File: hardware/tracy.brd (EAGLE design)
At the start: 100 x 80 mm, 67 parts, among them IC1 SIM900, J1 U.FL, J2 U.FL, Q4 si2305cd, T2 BC846, U1 SPX5205 3v3, U3 TC1014 2V8, Y1 32768Hz CFPX-217 12.5pF

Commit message: daily snapshot
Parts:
- moved C13 0.20 mm to (34.8, 26.4)
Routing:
- net N$42: track 0.00 -> 34.5 mm
- net N$43: track 0.00 -> 32.2 mm
- net SIM_VCC: track 3.80 -> 27.0 mm
- net SIMLOCK_IO: track 0.00 -> 19.5 mm
- net SIMLOCK_RST: track 0.00 -> 16.5 mm
- net SIMLOCK_CLK: track 0.00 -> 15.1 mm
- net N$17: track 0.00 -> 2.84 mm
- net N$19: track 0.00 -> 2.79 mm
- net N$18: track 0.00 -> 2.79 mm
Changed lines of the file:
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@@
 <element name="R15" library="rcl" package="R0805W" value="1k1" x="14.9" y="1.8" rot="R180"/>
 <element name="C12" library="rcl" package="C0805" value="4u7" x="34.8" y="23" rot="R180"/>
-<element name="C13" library="rcl" package="C0805" value="100n" x="34.8" y="26.6" rot="R180"/>
+<element name="C13" library="rcl" package="C0805" value="100n" x="34.8" y="26.4" rot="R180"/>
 <element name="C14" library="rcl" package="C0805" value="22p" x="38.9" y="35.1"/>
 <element name="R17" library="rcl" package="R0805W" value="10k" x="34.8" y="35.1" rot="R180"/>
@@
 <contactref element="U$6" pad="6"/>
 <contactref element="U$6" pad="TH"/>
-<polygon width="0.254" layer="1" isolate="0.254">
+<polygon width="0.254" layer="1" isolate="0.254" thermals="no">
 <vertex x="0.1" y="37.6"/>
 <vertex x="58.2" y="37.6"/>
@@
 <contactref element="U$8" pad="3"/>
 <wire x1="30.45" y1="27" x2="33.85" y2="27" width="0.254" layer="1"/>
-<wire x1="33.85" y1="27" x2="33.85" y2="26.6" width="0.254" layer="1"/>
+<wire x1="33.85" y1="27" x2="33.85" y2="26.4" width="0.254" layer="1"/>
 <contactref element="IC1" pad="30"/>
-<wire x1="33.1" y1="32.1" x2="49.01" y2="34" width="0" layer="19" extent="1-1"/>
-<wire x1="33.85" y1="27" x2="33.1" y2="32.1" width="0" layer="19" extent="1-1"/>
+<wire x1="33.1" y1="32.1" x2="33.1" y2="31.7" width="0.254" layer="1"/>
+<wire x1="33.1" y1="31.7" x2="33.3" y2="31.5" width="0.254" layer="1"/>
+<wire x1="33.3" y1="31.5" x2="35.4" y2="31.5" width="0.254" layer="1"/>
+<wire x1="34.75" y1="27.5" x2="33.85" y2="26.4" width="0.254" layer="1"/>
+<wire x1="49.01" y1="34" x2="49.01" y2="32.11" width="0.254" layer="1"/>
+<wire x1="49.01" y1="32.11" x2="47.8" y2="30.9" width="0.254" layer="1"/>
+<wire x1="47.8" y1="30.9" x2="38.1" y2="30.9" width="0.254" layer="1"/>
+<wire x1="38.1" y1="30.9" x2="37.5" y2="30.3" width="0.254" layer="1"/>
+<wire x1="37.5" y1="30.3" x2="37.5" y2="29" width="0.254" layer="1"/>
+<wire x1="37.5" y1="29" x2="36.6" y2="28.1" width="0.254" layer="1"/>
+<wire x1="36.6" y1="28.1" x2="36.1" y2="28.1" width="0.254" layer="1"/>
+<wire x1="36.1" y1="28.1" x2="35.5" y2="27.5" width="0.254" layer="1"/>
+<wire x1="35.5" y1="27.5" x2="34.75" y2="27.5" width="0.254" layer="1"/>
+<wire x1="37.5" y1="30.3" x2="35.4" y2="31.5" width="0" layer="19" extent="1-1"/>
 </signal>
 <signal name="SIMLOCK_CLK">
@@
 <contactref element="U$18" pad="2"/>
 <contactref element="U$8" pad="4"/>
-<wire x1="35" y1="32.1" x2="43.93" y2="34" width="0" layer="19" extent="1-1"/>
-<wire x1="34.8" y1="29.1" x2="35" y2="32.1" width="0" layer="19" extent="1-1"/>
+<wire x1="43.93" y1="34" x2="43.93" y2="32.53" width="0.254" layer="1"/>
+<wire x1="43.93" y1="32.53" x2="43.3" y2="31.9" width="0.254" layer="1"/>
+<wire x1="43.3" y1="31.9" x2="36.5" y2="31.9" width="0.254" layer="1"/>
+<wire x1="36.5" y1="31.9" x2="36.3" y2="32.1" width="0.254" layer="1"/>
+<wire x1="36.3" y1="32.1" x2="35" y2="32.1" width="0.254" layer="1"/>
+<wire x1="34.8" y1="29.1" x2="36.2" y2="29.1" width="0.254" layer="1"/>
+<wire x1="36.2" y1="29.1" x2="36.5" y2="29.4" width="0.254" layer="1"/>
+<wire x1="36.5" y1="29.4" x2="36.5" y2="31.9" width="0.254" layer="1"/>
 </signal>
 <signal name="SIMLOCK_RST">
@@
 <contactref element="U$18" pad="3"/>
 <contactref element="U$8" pad="6"/>
-<wire x1="35" y1="33.4" x2="46.47" y2="34" width="0" layer="19" extent="1-1"/>
+<wire x1="35" y1="33.4" x2="42.5" y2="33.4" width="0.254" layer="1"/>
+<wire x1="42.5" y1="33.4" x2="43" y2="33.9" width="0.254" layer="1"/>
+<wire x1="43" y1="33.9" x2="43" y2="35.5" width="0.254" layer="1"/>
+<wire x1="43" y1="35.5" x2="43.5" y2="36" width="0.254" layer="1"/>
+<wire x1="43.5" y1="36" x2="46.2" y2="36" width="0.254" layer="1"/>
+<wire x1="46.2" y1="36" x2="46.5" y2="35.7" width="0.254" layer="1"/>
+<wire x1="46.5" y1="35.7" x2="46.5" y2="34.03" width="0.254" layer="1"/>
+<wire x1="46.5" y1="34.03" x2="46.47" y2="34" width="0.254" layer="1"/>
+<wire x1="34.8" y1="29.9" x2="35.8" y2="29.9" width="0.254" layer="1"/>
+<wire x1="35.8" y1="29.9" x2="35.9" y2="30" width="0.254" layer="1"/>
 <wire x1="34.8" y1="29.9" x2="35" y2="33.4" width="0" layer="19" extent="1-1"/>
 </signal>
@@
 <contactref element="U$18" pad="1"/>
 <contactref element="U$8" pad="5"/>
-<wire x1="39.85" y1="35.1" x2="45.2" y2="34" width="0" layer="19" extent="1-1"/>
-<wire x1="35" y1="32.75" x2="39.85" y2="35.1" width="0" layer="19" extent="1-1"/>
-<wire x1="34.8" y1="28.225" x2="35" y2="32.75" width="0" layer="19" extent="1-1"/>
+<wire x1="45.2" y1="34" x2="45.2" y2="32.3" width="0.254" layer="1"/>
+<wire x1="45.2" y1="32.3" x2="44.3" y2="31.4" width="0.254" layer="1"/>
+<wire x1="44.3" y1="31.4" x2="37.2" y2="31.4" width="0.254" layer="1"/>
+<wire x1="37.2" y1="31.4" x2="37" y2="31.2" width="0.254" layer="1"/>
+<wire x1="37" y1="31.2" x2="37" y2="29.2" width="0.254" layer="1"/>
+<wire x1="37" y1="29.2" x2="36.4" y2="28.6" width="0.254" layer="1"/>
+<wire x1="36.4" y1="28.6" x2="35.9" y2="28.6" width="0.254" layer="1"/>
+<wire x1="35.9" y1="28.6" x2="35.5" y2="28.2" width="0.254" layer="1"/>
+<wire x1="35.5" y1="28.2" x2="34.825" y2="28.2" width="0.254" layer="1"/>
+<wire x1="34.825" y1="28.2" x2="34.8" y2="28.225" width="0.254" layer="1"/>
+<wire x1="35" y1="32.75" x2="39.55" y2="32.75" width="0.254" layer="1"/>
+<wire x1="39.55" y1="32.75" x2="39.85" y2="35.1" width="0" layer="19" extent="1-1"/>
+<wire x1="37" y1="31.2" x2="35" y2="32.75" width="0" layer="19" extent="1-1"/>
 </signal>
 <signal name="N$42">
@@
 <contactref element="U$8" pad="1"/>
 <contactref element="IC1" pad="34"/>
-<wire x1="33.1" y1="33.4" x2="33.7475" y2="35.1" width="0" layer="19" extent="1-1"/>
-<wire x1="30.45" y1="31" x2="33.1" y2="33.4" width="0" layer="19" extent="1-1"/>
-<wire x1="43.38" y1="2.9" x2="30.45" y2="31" width="0" layer="19" extent="1-1"/>
+<wire x1="30.45" y1="31" x2="30.45" y2="32.35" width="0.254" layer="1"/>
+<wire x1="30.45" y1="32.35" x2="31.5" y2="33.4" width="0.254" layer="1"/>
+<wire x1="31.5" y1="33.4" x2="33.1" y2="33.4" width="0.254" layer="1"/>
+<wire x1="33.1" y1="33.4" x2="33.1" y2="34.4525" width="0.254" layer="1"/>
+<wire x1="33.1" y1="34.4525" x2="33.7475" y2="35.1" width="0.254" layer="1"/>
+<wire x1="43.38" y1="2.9" x2="43.38" y2="25.52" width="0.254" layer="1"/>
+<wire x1="43.38" y1="25.52" x2="39.5" y2="29.4" width="0.254" layer="1"/>
+<wire x1="39.5" y1="29.4" x2="33.1" y2="33.4" width="0" layer="19" extent="1-1"/>
 </signal>
 <signal name="N$43">
 <contactref element="R17" pad="1"/>
 <contactref element="IC1" pad="15"/>
-<wire x1="25.2" y1="11.75" x2="35.8525" y2="35.1" width="0" layer="19" extent="1-1"/>
+<wire x1="25.2" y1="11.75" x2="25.2" y2="13" width="0.254" layer="1"/>
+<wire x1="25.2" y1="13" x2="28.2" y2="16" width="0.254" layer="1"/>
+<wire x1="28.2" y1="16" x2="28.2" y2="32" width="0.254" layer="1"/>
+<wire x1="28.2" y1="32" x2="32.8" y2="36.6" width="0.254" layer="1"/>
+<wire x1="32.8" y1="36.6" x2="35.3" y2="36.6" width="0.254" layer="1"/>
+<wire x1="35.3" y1="36.6" x2="35.8" y2="36.1" width="0.254" layer="1"/>
+<wire x1="35.8" y1="36.1" x2="35.8" y2="35.1525" width="0.254" layer="1"/>
+<wire x1="35.8" y1="35.1525" x2="35.8525" y2="35.1" width="0.254" layer="1"/>
 </signal>
 <signal name="PWRKEY">
@@
 <contactref element="U$18" pad="8"/>
 <contactref element="IC1" pad="31"/>
-<wire x1="30.45" y1="28" x2="33.2" y2="28.225" width="0" layer="19" extent="1-1"/>
+<wire x1="30.45" y1="28" x2="32.975" y2="28" width="0.254" layer="1"/>
+<wire x1="32.975" y1="28" x2="33.2" y2="28.225" width="0.254" layer="1"/>
 </signal>
 <signal name="N$18">
 <contactref element="U$18" pad="7"/>
 <contactref element="IC1" pad="32"/>
-<wire x1="30.45" y1="29" x2="33.2" y2="29.1" width="0" layer="19" extent="1-1"/>
+<wire x1="30.45" y1="29" x2="33.1" y2="29" width="0.254" layer="1"/>
+<wire x1="33.1" y1="29" x2="33.2" y2="29.1" width="0.254" layer="1"/>
 </signal>
 <signal name="N$19">
 <contactref element="U$18" pad="6"/>
 <contactref element="IC1" pad="33"/>
-<wire x1="30.45" y1="30" x2="33.2" y2="29.9" width="0" layer="19" extent="1-1"/>
+<wire x1="30.45" y1="30" x2="33.1" y2="30" width="0.254" layer="1"/>
+<wire x1="33.1" y1="30" x2="33.2" y2="29.9" width="0.254" layer="1"/>
 </signal>
 <signal name="PW_RAW">

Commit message: pcb done
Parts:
- removed LED3: orange, led:CHIP-LED0805
- removed R9: 10k, rcl:R0805W
- added LED1: green, led:CHIPLED_0805
- added R6: 100k, rcl:R0805W
- added R7: 470, rcl:R0805W
- R14: value NA/10k -> DNP 10k th
- U$17: value battery -> MOLEX_4HORIZONTAL
- U$19: value power_in -> MOLEX_4HORIZONTAL
- U2: value (none) -> 3339
- moved R1 60.5 mm to (38.2, 19.8), turned to 90 degrees
- moved R35 53.2 mm to (23.7, 22.6), turned to 0 degrees
- moved R34 52.8 mm to (24.7, 19.6)
- moved C10 52.4 mm to (5.60, 17.4), turned to 270 degrees
- moved U$20 51.5 mm to (34.4, 14.0)
- moved C17 49.5 mm to (7.70, 17.4), turned to 270 degrees
- moved C8 46.7 mm to (9.80, 17.4), turned to 270 degrees
- moved C24 45.7 mm to (13.0, 12.3), turned to 270 degrees
- moved C7 43.6 mm to (38.2, 15.6), turned to 270 degrees
- moved C23 42.7 mm to (15.1, 12.3), turned to 270 degrees
- moved Y1 42.0 mm to (14.1, 15.5), turned to 180 degrees
- moved U2 40.8 mm to (40.3, 31.5), turned to 180 degrees
- moved C9 40.2 mm to (12.7, 31.1), turned to 180 degrees
- moved R3 39.7 mm to (18.9, 10.9), turned to 180 degrees
- moved R4 37.9 mm to (18.9, 13.0), turned to 0 degrees
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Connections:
- net N$8 renamed GPS_VCC
- removed net N$21: LED3.C, U$6.9
- removed net N$22: LED3.A, R9.2
- removed net P1.0: U$1.14
- removed net P1.1: U$1.15
- removed net P1.2: U$1.16
- removed net P1.3: U$1.17
- removed net P1.4: U$1.18
- removed net P1.5: U$1.19
- removed net P1.6: U$1.20
- removed net P1.7: U$1.21
- removed net P2.0: U$1.22
- removed net P4.6: U$1.35
- removed net P4.7: U$1.36
- removed net P5.0: U$1.5
- removed net P5.1: U$1.6
- removed net P6.0: U$1.1
- removed net P6.1: C18.1, R22.2, R24.1, U$1.2
- removed net P6.2: C2.1, R3.2, R4.1, U$1.3
- removed net P6.3: U$1.4
- new net BAT_DIV: C2.1, R3.2, R4.1, U$1.4
- new net CH: R7.2, U$1.15
- new net N$10: R7.1, U$6.9
- new net N$8: LED1.C, R6.1
- new net PW_RAW_DIV: C18.1, R22.2, R24.1, U$1.3
- new net STATUS: LED1.A, U$1.16
- net 3V3_EN: now also U$1.1
- net 5V: now also U$17.4; no longer U$19.4
- net BAT: now also U$19.1; no longer U$17.4
- net CE: now also U$1.2
- net CTS: now also U$1.19
- net DTR: now also U$1.17
- net GND: now also R6.2, U$19.2; no longer U$17.2
- net GPRS_EN: now also U$1.21
- net GPRS_POW: now also U$1.22
- net N$12: now also U$17.2; no longer U$19.2
- net P4.0: now also U$20.5; no longer U$20.6
- net P4.1: now also U$20.6; no longer U$20.5
- net PW_EN: now also U$1.36
- net PW_RAW: now also U$17.1; no longer U$19.1
- net RI: now also U$1.18
- net RTS: now also U$1.20
- net TS: now also U$19.4; no longer U$17.1
- net VBACKUP: now also U$1.35
- net VIN: no longer R9.1
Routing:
- net 2V8: track 0.00 -> 70.7 mm, vias 0 -> 7
- net PW_EN: track 0.00 -> 38.9 mm
- net VIN: track 33.4 -> 70.6 mm, vias 0 -> 3
- net 3V3_EN: track 0.00 -> 36.2 mm, vias 0 -> 2
- net GPRS_RX: track 0.00 -> 31.5 mm, vias 0 -> 1
- net VBACKUP: track 0.00 -> 30.9 mm
- net GPRS_TX: track 0.00 -> 29.2 mm, vias 0 -> 1
- net GPRS_POW: track 0.00 -> 28.6 mm, vias 0 -> 1
- net GPS_RX: track 0.00 -> 25.8 mm
- net GPS_TX: track 0.00 -> 24.7 mm
- net CE: track 0.00 -> 24.4 mm, vias 0 -> 3
- net P4.0: track 0.00 -> 24.1 mm, vias 0 -> 2
- net P4.1: track 0.00 -> 22.9 mm, vias 0 -> 2
- net GPS_VCC: track 0.00 -> 20.4 mm
- net TEST: track 0.00 -> 19.0 mm, vias 0 -> 1
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- added copper zone on layer 16, net GND
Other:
- board size 100 x 80 mm -> 58.5 x 38 mm

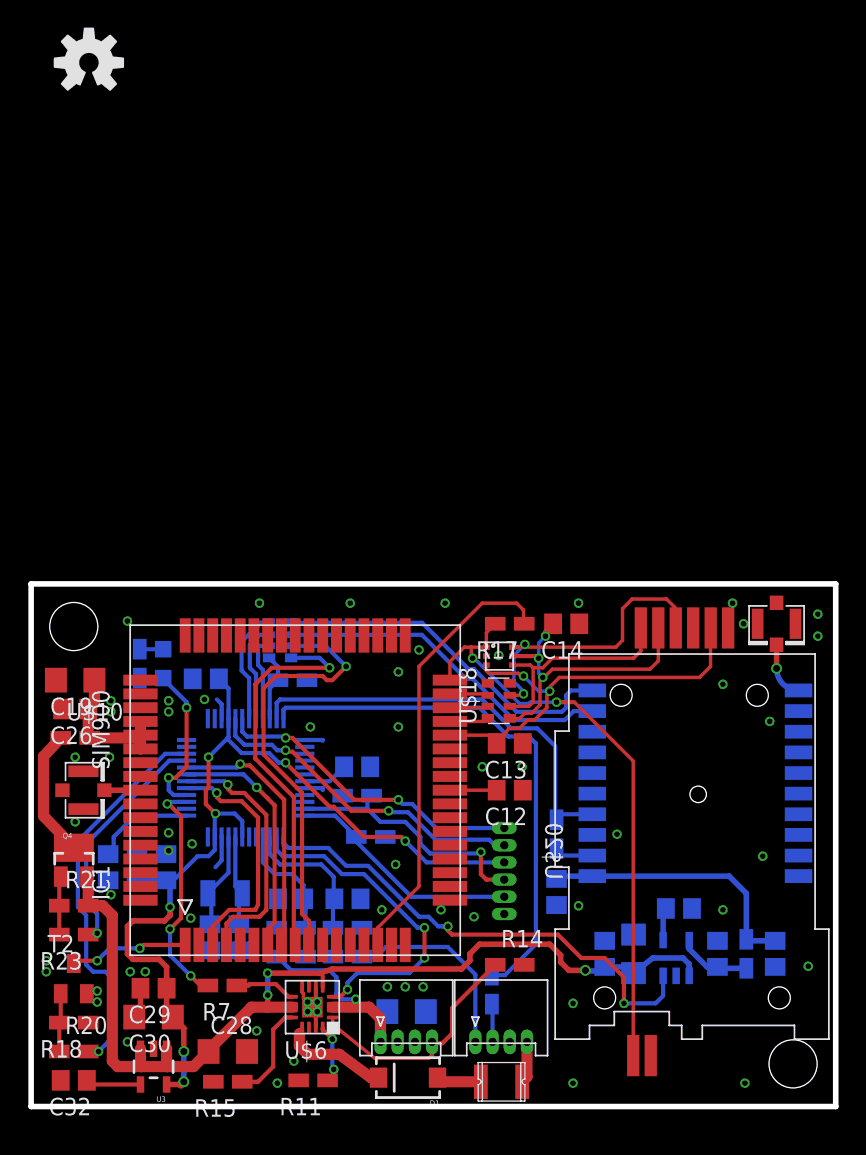
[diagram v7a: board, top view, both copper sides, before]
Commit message: add silkscreen
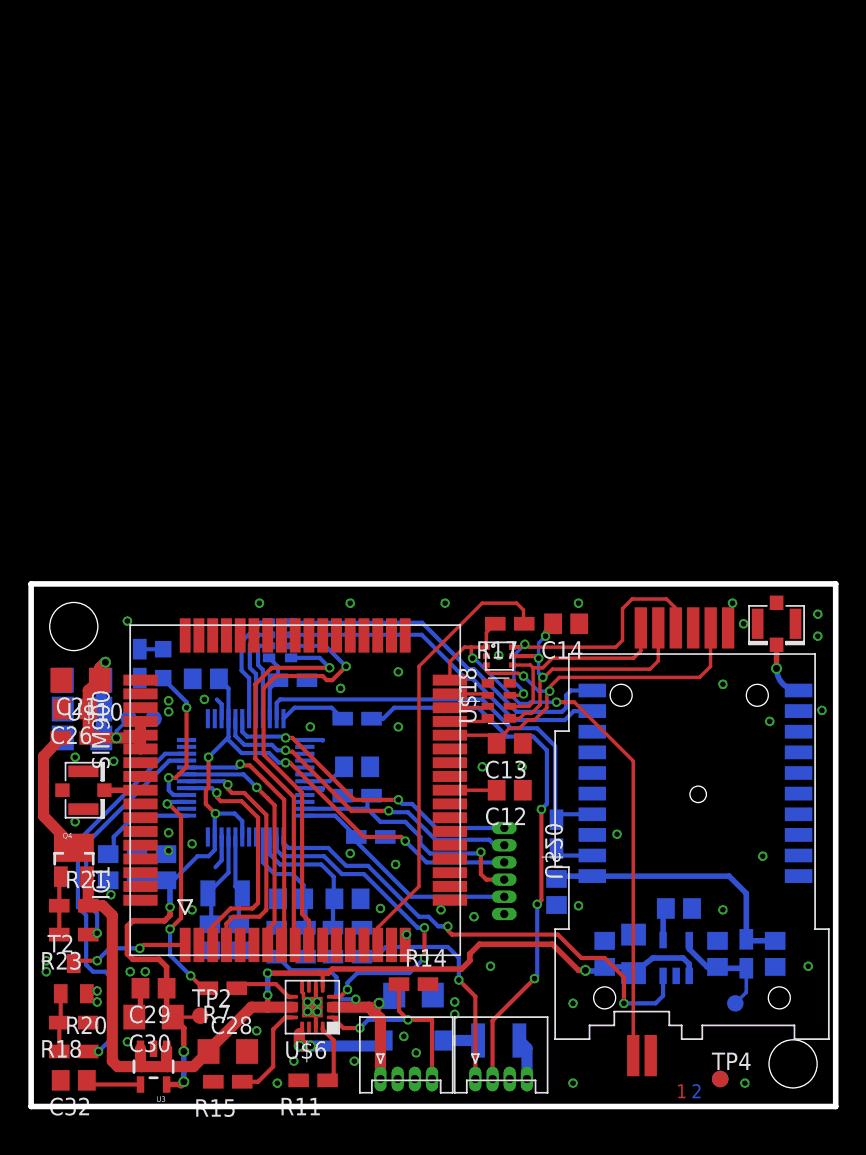
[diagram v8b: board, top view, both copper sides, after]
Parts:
- removed C19: 47uF, rcl:C1206
- added C15, C16, C20, C21: 100uF, rcl:C1206
- added TP1, TP2, TP3, TP4, TP5, TP6: TPTP12R, testpad:TP12R
- U$17: value MOLEX_4HORIZONTAL -> 5V
- U$19: value MOLEX_4HORIZONTAL -> LiPo
- U$20: value MOLEX_6VERTICAL -> prog
- moved U$7 73.7 mm to (34.8, 8.90), flipped to the bottom
- moved R5 22.0 mm to (23.7, 28.2), turned to 0 degrees
- moved R14 7.14 mm to (27.8, 8.90)
- moved U$9 3.01 mm to (34.0, 4.80), flipped to the bottom, turned to 0 degrees
- moved D1 2.73 mm to (27.8, 4.80), flipped to the bottom, turned to 0 degrees
- moved U$17 2.70 mm to (32.3, 2.00)
- moved U$19 2.70 mm to (25.4, 2.00)
- moved C27 1.30 mm to (27.8, 8.10)
- moved R7 0.20 mm to (13.9, 8.60)
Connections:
- net +3V3: now also TP3.TP
- net 2V8: now also TP2.TP
- net GND: now also C15.2, C16.2, C20.2, C21.2, TP4.TP, TP5.TP, TP6.TP; no longer C19.2
- net VBAT: now also C15.1, C16.1, C20.1, C21.1, TP1.TP; no longer C19.1
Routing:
- net N$12: track 2.77 -> 39.9 mm, vias 0 -> 3
- net PW_EN: track 38.9 -> 4.96 mm
- net VBAT: track 11.2 -> 20.3 mm, vias 0 -> 2
- net +3V3: track 5.38 -> 8.26 mm
- net TS: track 17.7 -> 15.0 mm, vias 0 -> 2
- net BAT: track 17.9 -> 20.6 mm, vias 1 -> 2
- net PW_RAW: track 14.3 -> 17.0 mm, vias 0 -> 1
- net 2V8: track 70.7 -> 72.7 mm
- net N$20: track 3.27 -> 2.55 mm
- net 5V_IN: track 8.11 -> 8.37 mm, vias 0 -> 2
- net N$27: vias 2 -> 0
- net GND: vias 60 -> 64
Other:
- board text added: "+2V8"
- board text added: "+3V3"
- board text added: "1"
- board text added: "2"
- board text added: "5V"
- board text added: "Vbat"
- board text added: "bat"
- board text added: "debug"
- board text added: "github.com/rodan/tracy"
- board text added: "gps"
- board text added: "gsm"
- board text added: "peter 201401 rev1"
- board text added: "status"
